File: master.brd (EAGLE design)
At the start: 56.1 x 93.9 mm, 76 parts, among them M1 DHT22-NP, M2 NRF24L01P-M, Q1 IRLML2502, Q3 25MHz, U1 XMEGA-A3TQFP, U2 DS1302SOIC, U3 25LC640A-E/SN, U4 ENC28J60SO, U5 TS1117, X1 serial, X2 SPI/1W, X3 I2C, X4 ADC, X6 PS25_3W-R, X7 PS25_3W-R, X8 PS25_3W-R, X9 PS25_3W-R

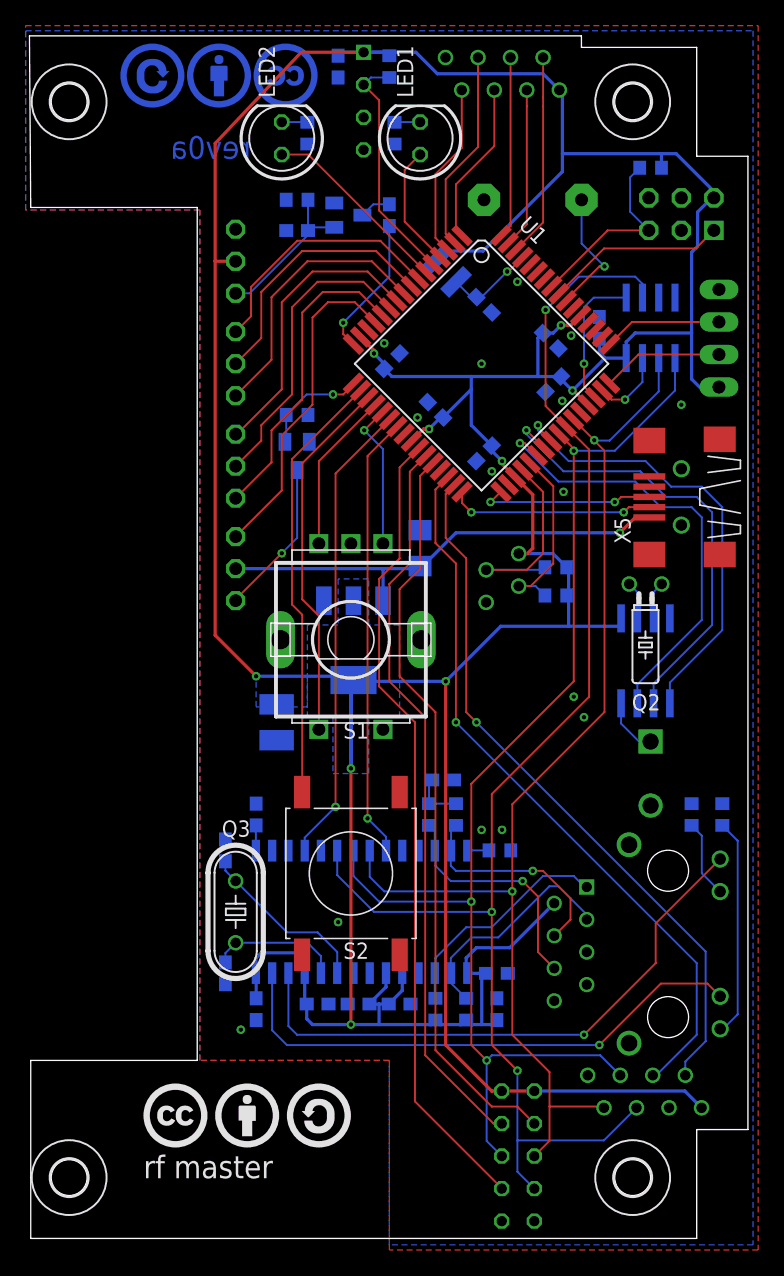
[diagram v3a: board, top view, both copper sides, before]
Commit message: moved x3 to the right
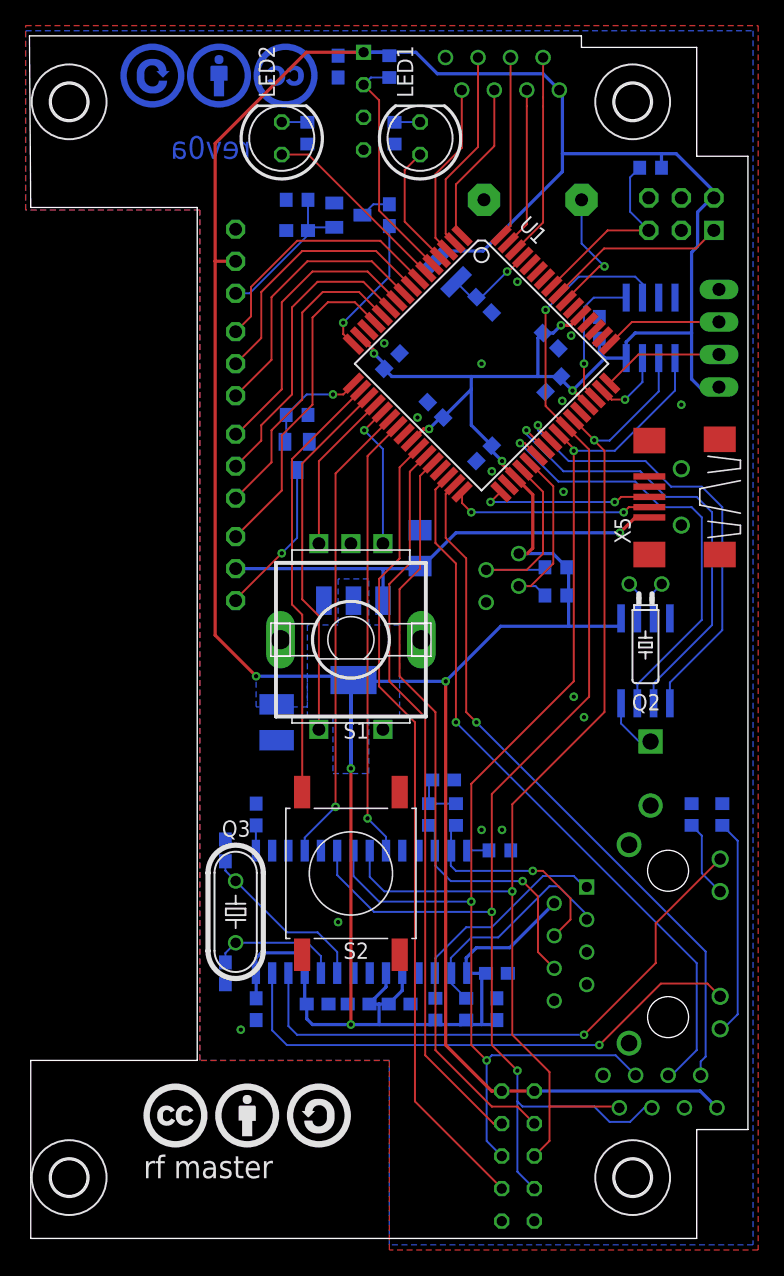
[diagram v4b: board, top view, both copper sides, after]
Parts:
- moved X2 1.20 mm to (49.1, 12.0)
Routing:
- net MISO: track 110.0 -> 111.3 mm
- net SCK: track 90.4 -> 91.6 mm
- net MOSI: track 96.8 -> 98.0 mm
- net VCC: track 373.2 -> 374.3 mm
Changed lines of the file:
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@@
 <layer number="38" name="bTest" color="7" fill="1" visible="no" active="yes"/>
 <layer number="39" name="tKeepout" color="4" fill="11" visible="no" active="yes"/>
-<layer number="40" name="bKeepout" color="1" fill="11" visible="no" active="yes"/>
+<layer number="40" name="bKeepout" color="1" fill="11" visible="yes" active="yes"/>
 <layer number="41" name="tRestrict" color="4" fill="10" visible="no" active="yes"/>
 <layer number="42" name="bRestrict" color="1" fill="10" visible="no" active="yes"/>
@@
 <layer number="45" name="Holes" color="7" fill="1" visible="no" active="yes"/>
 <layer number="46" name="Milling" color="3" fill="1" visible="no" active="yes"/>
-<layer number="47" name="Measures" color="7" fill="1" visible="no" active="yes"/>
+<layer number="47" name="Measures" color="7" fill="1" visible="yes" active="yes"/>
 <layer number="48" name="Document" color="7" fill="1" visible="no" active="yes"/>
 <layer number="49" name="Reference" color="7" fill="1" visible="no" active="yes"/>
@@
 <text x="17.2" y="84.8" size="1.778" layer="16" font="vector" ratio="10" rot="MR0">&gt;BR</text>
 <text x="8.8" y="2.8" size="1.778" layer="21">&gt;BR</text>
+<dimension x1="6.8" y1="-1.2" x2="36.8" y2="-1.2" x3="21.8" y3="-6.4" textsize="1.778" layer="47"/>
 </plain>
 <attributes>
@@
 <attribute name="VALUE" x="41.635" y="48.165" size="1.27" layer="28" rot="MR0"/>
 </element>
-<element name="X2" library="con-amp-micromatch" package="MICROMATCH-8" value="SPI/1W" x="47.935" y="11.97" smashed="yes" rot="MR180">
-<attribute name="NAME" x="41.79" y="9.23" size="1.27" layer="26" rot="MR180"/>
-<attribute name="VALUE" x="43.49" y="15.78" size="1.27" layer="28" rot="MR180"/>
+<element name="X2" library="con-amp-micromatch" package="MICROMATCH-8" value="SPI/1W" x="49.135" y="11.97" smashed="yes" rot="MR180">
+<attribute name="NAME" x="42.99" y="9.23" size="1.27" layer="26" rot="MR180"/>
+<attribute name="VALUE" x="44.69" y="15.78" size="1.27" layer="28" rot="MR180"/>
 </element>
 <element name="X3" library="con-amp-micromatch" package="MICROMATCH-4" value="I2C" x="36.83" y="52.07" smashed="yes" rot="MR90">
@@
 <wire x1="36" y1="35.2" x2="43.6" y2="42.8" width="0.1524" layer="1"/>
 <via x="38" y="13.6" extent="1-16" drill="0.3302" shape="octagon"/>
-<wire x1="38" y1="13.6" x2="38" y2="8.155" width="0.1524" layer="16"/>
-<wire x1="38" y1="8.155" x2="38" y2="5.71" width="0.1524" layer="16"/>
+<wire x1="38" y1="13.6" x2="38" y2="11.2" width="0.1524" layer="16"/>
+<wire x1="38" y1="11.2" x2="38" y2="5.71" width="0.1524" layer="16"/>
 <wire x1="38" y1="5.71" x2="39.32" y2="4.39" width="0.1524" layer="16"/>
-<wire x1="47.3" y1="10.7" x2="44.755" y2="8.155" width="0.1524" layer="16"/>
-<wire x1="44.755" y1="8.155" x2="38" y2="8.155" width="0.1524" layer="16"/>
+<wire x1="38" y1="11.2" x2="38.4" y2="10.8" width="0.1524" layer="16"/>
+<wire x1="38.4" y1="10.8" x2="44" y2="10.8" width="0.1524" layer="16"/>
+<wire x1="44" y1="10.8" x2="45.2" y2="9.6" width="0.1524" layer="16"/>
+<wire x1="45.2" y1="9.6" x2="46.8" y2="9.6" width="0.1524" layer="16"/>
+<wire x1="46.8" y1="9.6" x2="47.9" y2="10.7" width="0.1524" layer="16"/>
+<wire x1="47.9" y1="10.7" x2="48.5" y2="10.7" width="0.1524" layer="16"/>
 </signal>
 <signal name="MOSI">
@@
 <wire x1="35.6" y1="8.11" x2="36.78" y2="6.93" width="0.1524" layer="16"/>
 <wire x1="35.6" y1="14.4" x2="36" y2="14.8" width="0.1524" layer="16"/>
-<wire x1="36" y1="14.8" x2="44.47" y2="14.8" width="0.1524" layer="16"/>
-<wire x1="44.47" y1="14.8" x2="46.03" y2="13.24" width="0.1524" layer="16"/>
+<wire x1="36" y1="14.8" x2="45.67" y2="14.8" width="0.1524" layer="16"/>
+<wire x1="45.67" y1="14.8" x2="47.23" y2="13.24" width="0.1524" layer="16"/>
 </signal>
 <signal name="SCK">
@@
 <wire x1="40.507103125" y1="13.492896875" x2="40.507103125" y2="10.8" width="0.1524" layer="1"/>
 <wire x1="40.507103125" y1="10.8" x2="40.507103125" y2="8.117103125" width="0.1524" layer="1"/>
-<wire x1="44.76" y1="10.7" x2="44.66" y2="10.8" width="0.1524" layer="1"/>
-<wire x1="44.66" y1="10.8" x2="40.507103125" y2="10.8" width="0.1524" layer="1"/>
+<wire x1="45.96" y1="10.7" x2="45.86" y2="10.8" width="0.1524" layer="1"/>
+<wire x1="45.86" y1="10.8" x2="40.507103125" y2="10.8" width="0.1524" layer="1"/>
 <wire x1="40.507103125" y1="8.117103125" x2="39.32" y2="6.93" width="0.1524" layer="1"/>
 </signal>
@@
 <wire x1="34" y1="53.6" x2="34" y2="41.6" width="0.1524" layer="1"/>
 <contactref element="X2" pad="2"/>
-<wire x1="52.7" y1="22.9" x2="52.7" y2="15.9" width="0.1524" layer="16"/>
-<wire x1="52.7" y1="15.9" x2="51.11" y2="14.31" width="0.1524" layer="16"/>
-<wire x1="51.11" y1="14.31" x2="51.11" y2="13.24" width="0.1524" layer="16"/>
+<wire x1="52.7" y1="22.9" x2="52.7" y2="14.7" width="0.1524" layer="16"/>
+<wire x1="52.7" y1="14.7" x2="52.31" y2="14.31" width="0.1524" layer="16"/>
+<wire x1="52.31" y1="14.31" x2="52.31" y2="13.24" width="0.1524" layer="16"/>
 <wire x1="34" y1="41.6" x2="34.8" y2="40.8" width="0.1524" layer="1"/>
 <wire x1="34.8" y1="40.8" x2="52.7" y2="22.9" width="0.1524" layer="16"/>
@@
 <via x="33.2" y="40.8" extent="1-16" drill="0.3302" shape="octagon"/>
 <wire x1="33.2" y1="40.8" x2="52" y2="22" width="0.1524" layer="16"/>
-<wire x1="52" y1="22" x2="52" y2="16.4" width="0.1524" layer="16"/>
-<wire x1="52" y1="16.4" x2="48.84" y2="13.24" width="0.1524" layer="16"/>
-<wire x1="48.84" y1="13.24" x2="48.57" y2="13.24" width="0.1524" layer="16"/>
+<wire x1="52" y1="22" x2="52" y2="15.2" width="0.1524" layer="16"/>
+<wire x1="52" y1="15.2" x2="50.04" y2="13.24" width="0.1524" layer="16"/>
+<wire x1="50.04" y1="13.24" x2="49.77" y2="13.24" width="0.1524" layer="16"/>
 </signal>
 <signal name="BUZZ">
@@
 <wire x1="27.73" y1="93.12" x2="28" y2="92.85" width="0.254" layer="16"/>
 <wire x1="42.94281875" y1="72.58301875" x2="42.980934375" y2="72.58301875" width="0.254" layer="1"/>
-<wire x1="14.4" y1="86" x2="21.12" y2="93.12" width="0.254" layer="1"/>
-<wire x1="21.12" y1="93.12" x2="25.99" y2="93.12" width="0.254" layer="1"/>
 <contactref element="X6" pad="2"/>
 <wire x1="14.4" y1="86" x2="14.4" y2="76.8" width="0.254" layer="1"/>
@@
 <wire x1="36.01" y1="12.01" x2="36.78" y2="12.01" width="0.254" layer="1"/>
 <wire x1="36.78" y1="12.01" x2="39.32" y2="12.01" width="0.254" layer="1"/>
-<wire x1="39.32" y1="12.01" x2="51.07" y2="12.01" width="0.254" layer="16"/>
-<wire x1="51.07" y1="12.01" x2="52.38" y2="10.7" width="0.254" layer="16"/>
+<wire x1="39.32" y1="12.01" x2="52.27" y2="12.01" width="0.254" layer="16"/>
+<wire x1="52.27" y1="12.01" x2="53.58" y2="10.7" width="0.254" layer="16"/>
+<wire x1="14.4" y1="86" x2="21.52" y2="93.12" width="0.254" layer="1"/>
+<wire x1="21.52" y1="93.12" x2="25.99" y2="93.12" width="0.254" layer="1"/>
 </signal>
 <signal name="!EEPHOLD">

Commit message: added sd card interface
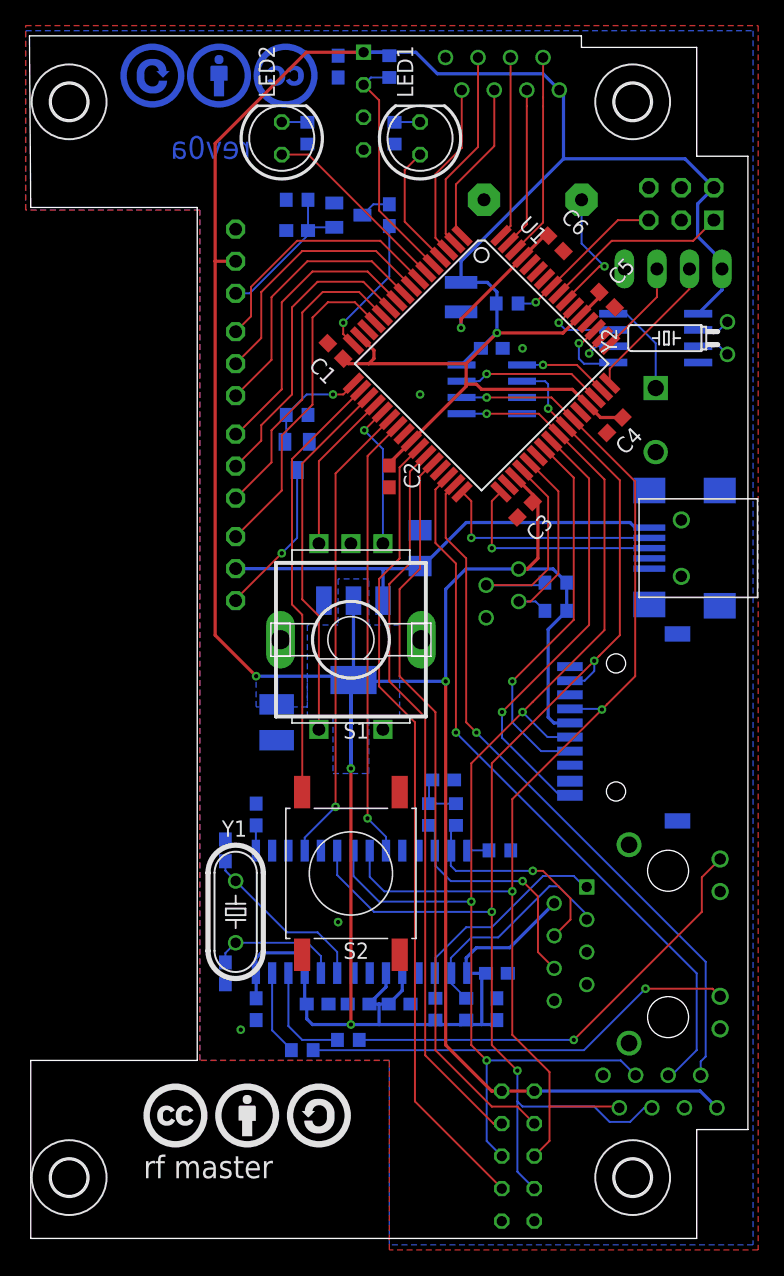
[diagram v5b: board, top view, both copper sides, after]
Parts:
- removed Q2: (no value), crystal:TC26H
- added SD1: MICROSD_SW, sd:MICROSD_SMD_EXTPIN
- added Y2: (no value), crystal:TC26H
- moved R14 37.6 mm to (21.2, 15.2), turned to 180 degrees
- moved R15 32.1 mm to (24.8, 16.0), turned to 180 degrees
- moved C14 27.6 mm to (48.8, 64.4)
- moved U2 25.2 mm to (48.8, 70.8), turned to 270 degrees
- moved R1 15.4 mm to (37.2, 73.5), turned to 0 degrees
- moved U3 13.3 mm to (36.0, 66.8), turned to 0 degrees
- moved C12 8.55 mm to (36.0, 70.0), turned to 180 degrees
- moved C6 7.38 mm to (41.0, 78.2), flipped to the top, turned to 315 degrees
- moved X1 6.48 mm to (50.2, 76.2), turned to 0 degrees
- moved C2 6.32 mm to (28.0, 60.0), flipped to the top, turned to 270 degrees
- moved C4 5.77 mm to (45.6, 64.0), flipped to the top, turned to 225 degrees
- moved C3 5.44 mm to (38.6, 57.4), flipped to the top, turned to 225 degrees
- moved C5 5.44 mm to (45.0, 73.8), flipped to the top, turned to 315 degrees
- moved C1 4.47 mm to (23.8, 69.8), flipped to the top
- moved X5 4.00 mm to (50.8, 54.4), flipped to the bottom, turned to 0 degrees
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- renumbered Q3 to Y1
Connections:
- new net !SDCS: SD1.2, U1.39
- new net SDCD: SD1.CD2, U1.40
- net !EEPCS: now also U1.47; no longer U1.46
- net !EEPHOLD: now also U1.46; no longer U1.47
- net GND: now also LAN1.LED1.2, LAN1.LED2.2, SD1.6, SD1.CD1, SD1.NC1, SD1.NC2; no longer R14.2, R15.2
- net MISO: now also SD1.7
- net MOSI: now also SD1.3
- net N$1: now also Y2.2; no longer Q2.2
- net N$21: now also R14.1; no longer LAN1.LED2.1
- net N$22: now also R15.1; no longer LAN1.LED1.1
- net N$23: now also LAN1.LED2.1, R14.2; no longer LAN1.LED2.2, R14.1
- net N$24: now also LAN1.LED1.1, R15.2; no longer LAN1.LED1.2, R15.1
- net N$3: now also Y2.1; no longer Q2.1
- net RTC_CE: now also U1.51; no longer U1.40
- net RTC_CLK: now also U1.54; no longer U1.38
- net RTC_IO: now also U1.50; no longer U1.39
- net SCK: now also SD1.5
- net VCC: now also SD1.4
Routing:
- net N$22: track 45.6 -> 8.42 mm, vias 1 -> 0
- net N$21: track 42.3 -> 6.64 mm, vias 1 -> 0
- net SDCD: track 0.00 -> 34.5 mm, vias 0 -> 1
- net RTC_IO: track 36.1 -> 3.84 mm
- net RTC_CE: track 36.0 -> 5.80 mm
- net !SDCS: track 0.00 -> 29.8 mm, vias 0 -> 1
- net N$24: track 6.09 -> 35.6 mm, vias 0 -> 1
- net RTC_CLK: track 35.0 -> 6.13 mm
- net N$23: track 17.1 -> 34.0 mm, vias 0 -> 1
- net VCC: track 374.3 -> 385.7 mm, vias 9 -> 5
- net MISO: track 111.3 -> 102.6 mm, vias 3 -> 4
- net !EEPHOLD: track 5.86 -> 11.4 mm
- net SCK: track 91.6 -> 96.3 mm, vias 2 -> 3
- net N$15: track 6.98 -> 11.4 mm
- net !EEPCS: track 11.0 -> 7.10 mm
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
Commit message: oshw logo, drc errors fixed
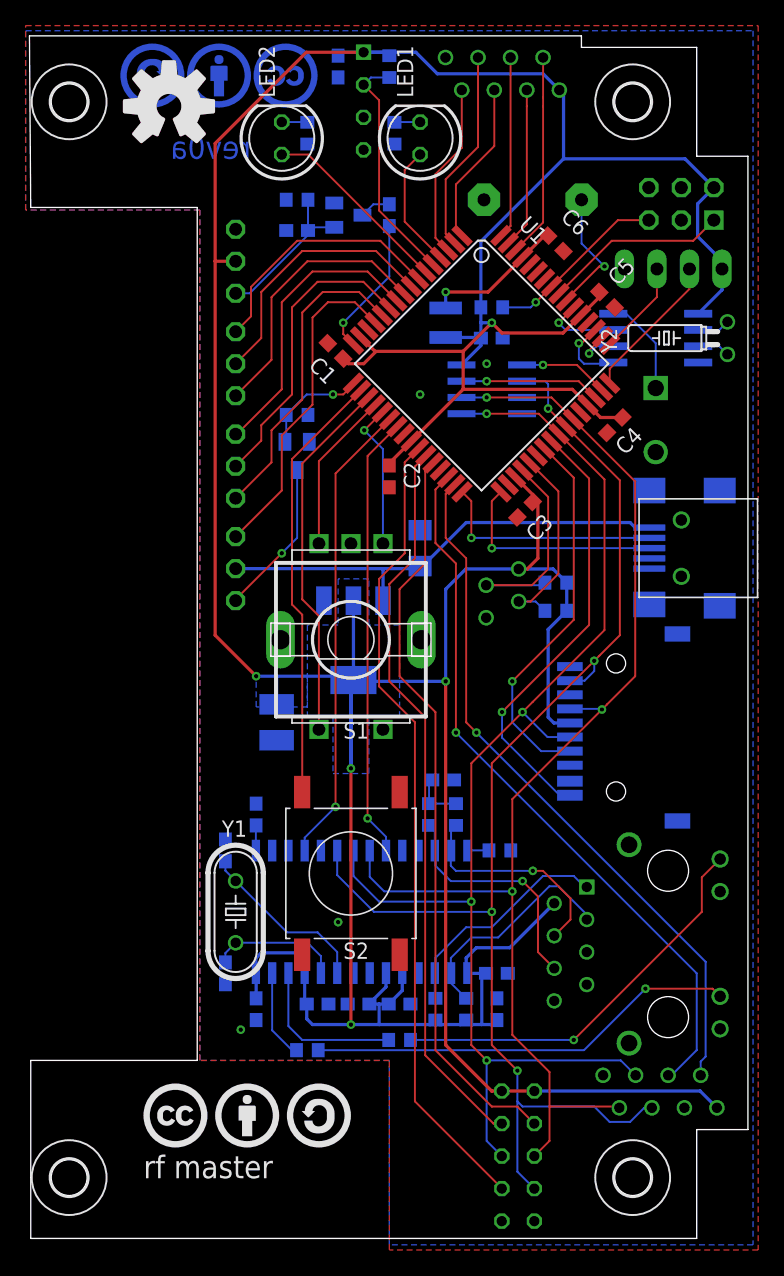
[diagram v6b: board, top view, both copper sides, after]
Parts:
- moved R15 4.00 mm to (28.8, 16.0)
- moved L1 2.33 mm to (32.4, 72.0), turned to 270 degrees
- moved R1 1.24 mm to (36.0, 73.2)
- moved C12 0.80 mm to (36.0, 70.8)
- moved R14 0.40 mm to (21.6, 15.2)
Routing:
- net N$28: track 0.00 -> 33.1 mm
- net N$22: track 8.42 -> 12.4 mm
- net N$24: track 35.6 -> 31.6 mm
- net N$11: track 12.9 -> 14.2 mm
- net VCC: track 385.7 -> 385.0 mm
